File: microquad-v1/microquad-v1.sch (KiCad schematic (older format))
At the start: 20 parts

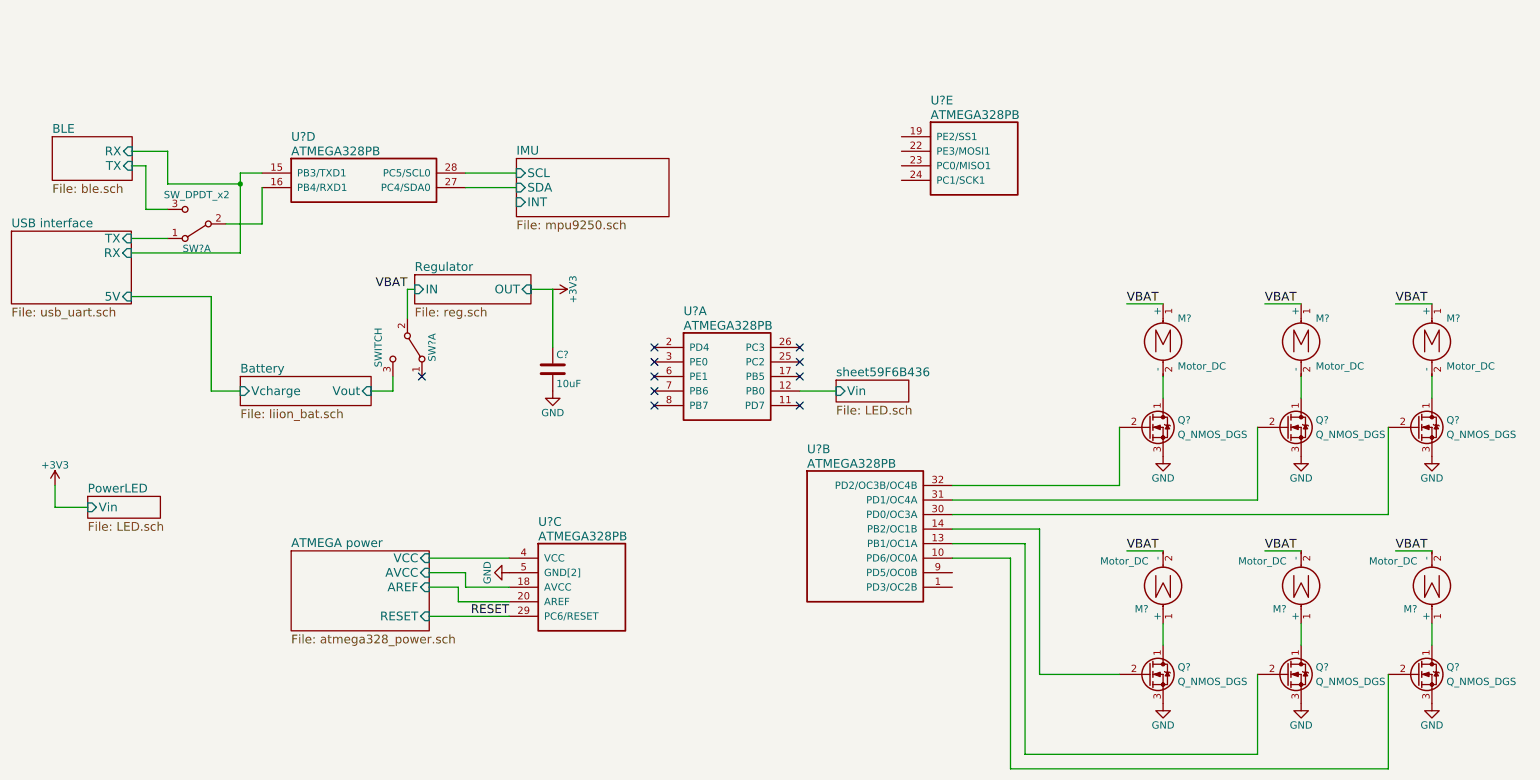
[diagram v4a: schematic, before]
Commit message: Moved LED to pin PB5
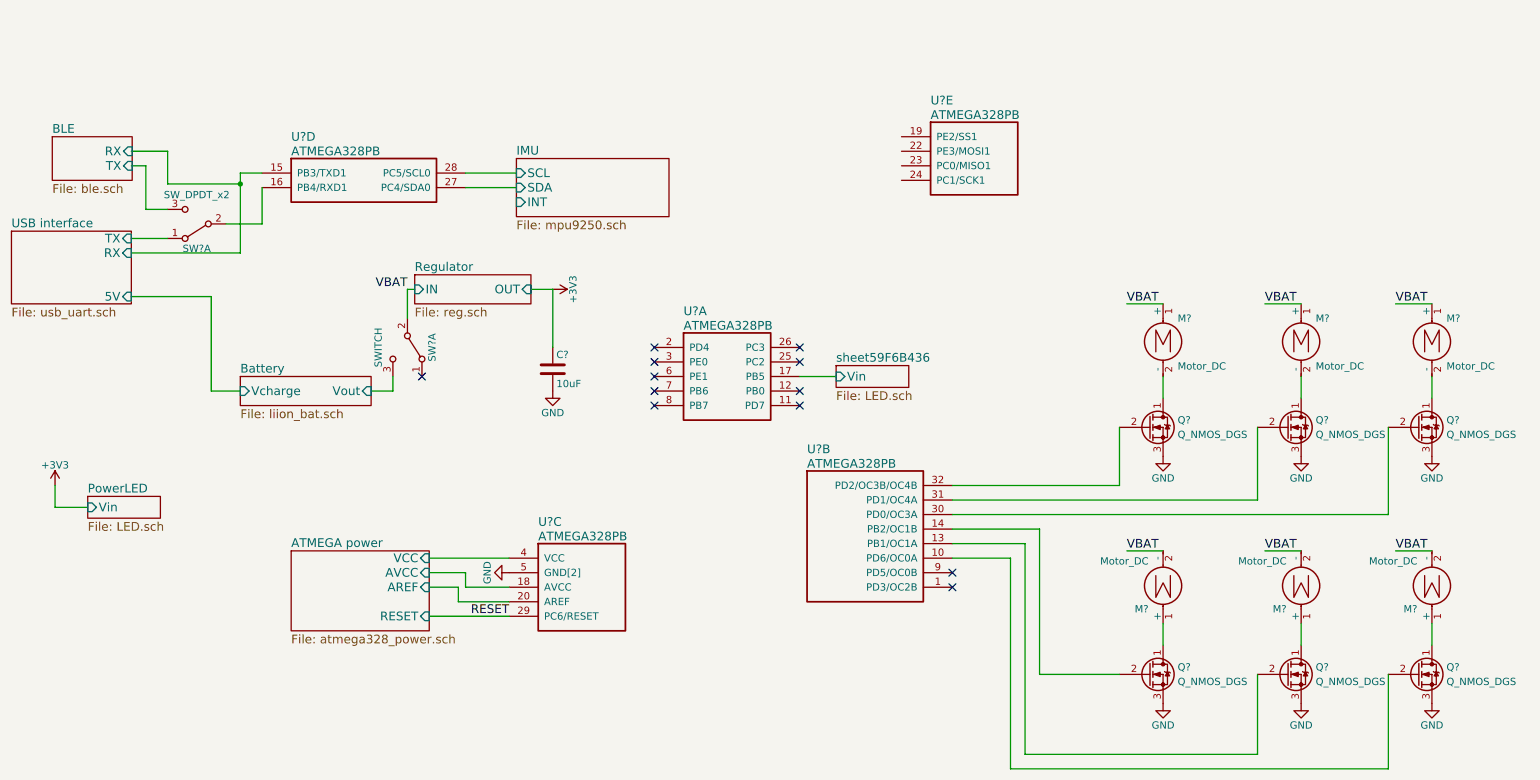
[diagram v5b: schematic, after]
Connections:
- wire segments 64 -> 63
- no-connect marks 10 -> 12
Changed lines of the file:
@@
 $Descr A4 11693 8268
 encoding utf-8
-Sheet 1 8
+Sheet 1 9
 Title ""
 Date ""
@@
 	10500 5000 10500 5150
 Wire Wire Line
-	6150 3400 6400 3400
-Wire Wire Line
 	8350 3650 8350 4050
 Wire Wire Line
@@
 	1800 1975 2300 1975
 Wire Wire Line
-	2300 1900 2300 1975
-Wire Wire Line
-	2300 1975 2300 2450
+	2300 1900 2300 2450
 Wire Wire Line
 	2300 1900 2450 1900
@@
 $EndSheet
 $Sheet
-S 6400 3325 500  150
+S 6400 3225 500  150
 U 59F6B438
 F0 "sheet59F6B436" 60
 F1 "LED.sch" 60
-F2 "Vin" I L 6400 3400 60
+F2 "Vin" I L 6400 3300 60
 $EndSheet
 $Comp
@@
 NoConn ~ 6150 3100
 NoConn ~ 6150 3200
-NoConn ~ 6150 3300
 NoConn ~ 6150 3500
 NoConn ~ 5150 3500
@@
 F4 "INT" I L 4200 2100 60
 $EndSheet
+NoConn ~ 7200 4650
+NoConn ~ 7200 4750
+NoConn ~ 6150 3400
+Wire Wire Line
+	6150 3300 6400 3300
 $EndSCHEMATC

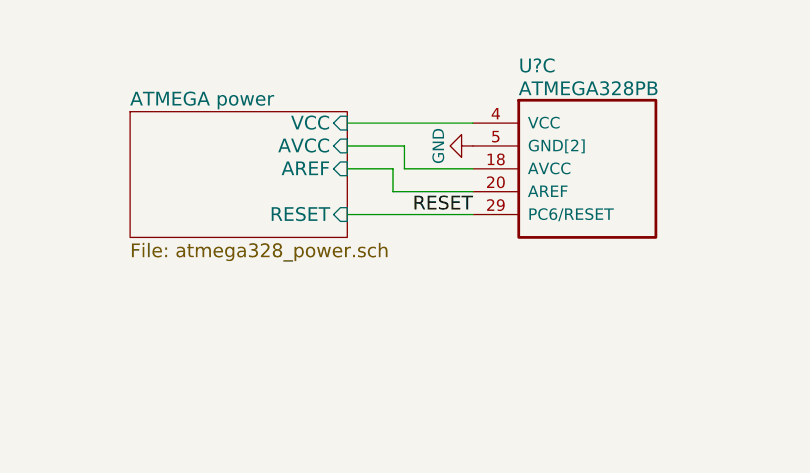
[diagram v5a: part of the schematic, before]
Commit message: Added reset button
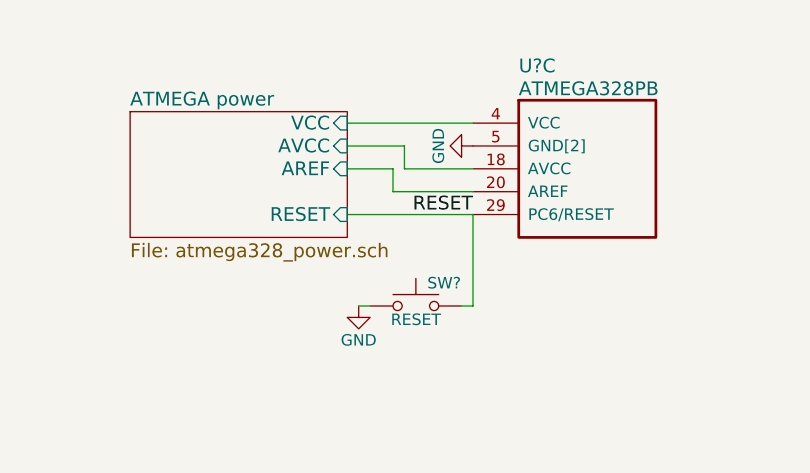
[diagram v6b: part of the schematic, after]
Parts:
- added SW?: RESET, symbol SW_Push
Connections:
- wire segments 63 -> 66
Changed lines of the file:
@@
 Wire Wire Line
 	6150 3300 6400 3300
+$Comp
+L SW_Push SW?
+U 1 1 59F7EEE0
+P 3900 5350
+F 0 "SW?" H 3950 5450 50  0000 L CNN
+F 1 "RESET" H 3900 5290 50  0000 C CNN
+F 2 "" H 3900 5550 50  0001 C CNN
+F 3 "" H 3900 5550 50  0001 C CNN
+	1    3900 5350
+	1    0    0    -1
+$EndComp
+$Comp
+L GND #PWR?
+U 1 1 59F7EFD3
+P 3650 5350
+F 0 "#PWR?" H 3650 5100 50  0001 C CNN
+F 1 "GND" H 3650 5200 50  0000 C CNN
+F 2 "" H 3650 5350 50  0001 C CNN
+F 3 "" H 3650 5350 50  0001 C CNN
+	1    3650 5350
+	1    0    0    -1
+$EndComp
+Wire Wire Line
+	3650 5350 3700 5350
+Wire Wire Line
+	4150 4950 4150 5350
+Wire Wire Line
+	4150 5350 4100 5350
 $EndSCHEMATC

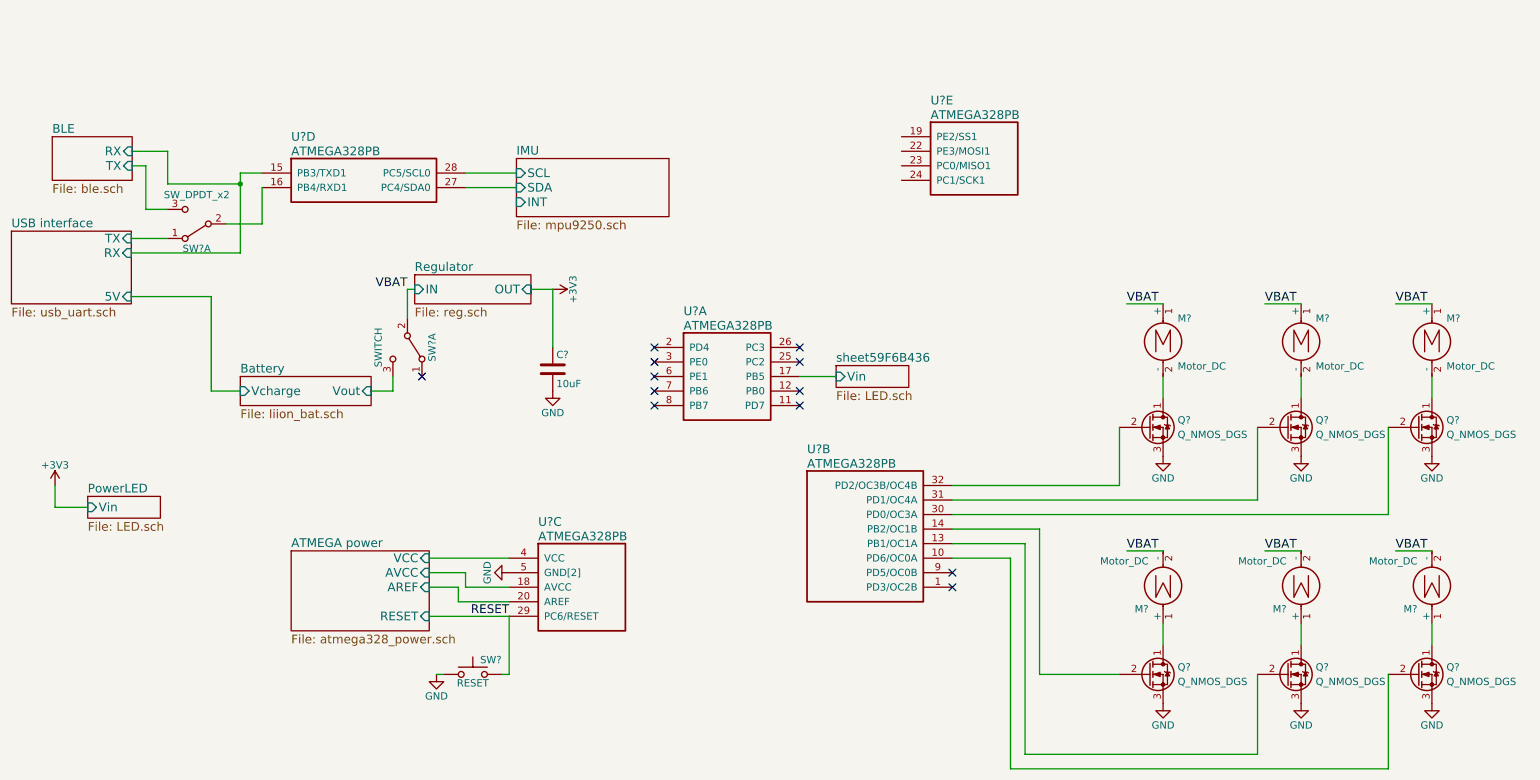
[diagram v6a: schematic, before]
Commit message: Added IMU interrupt
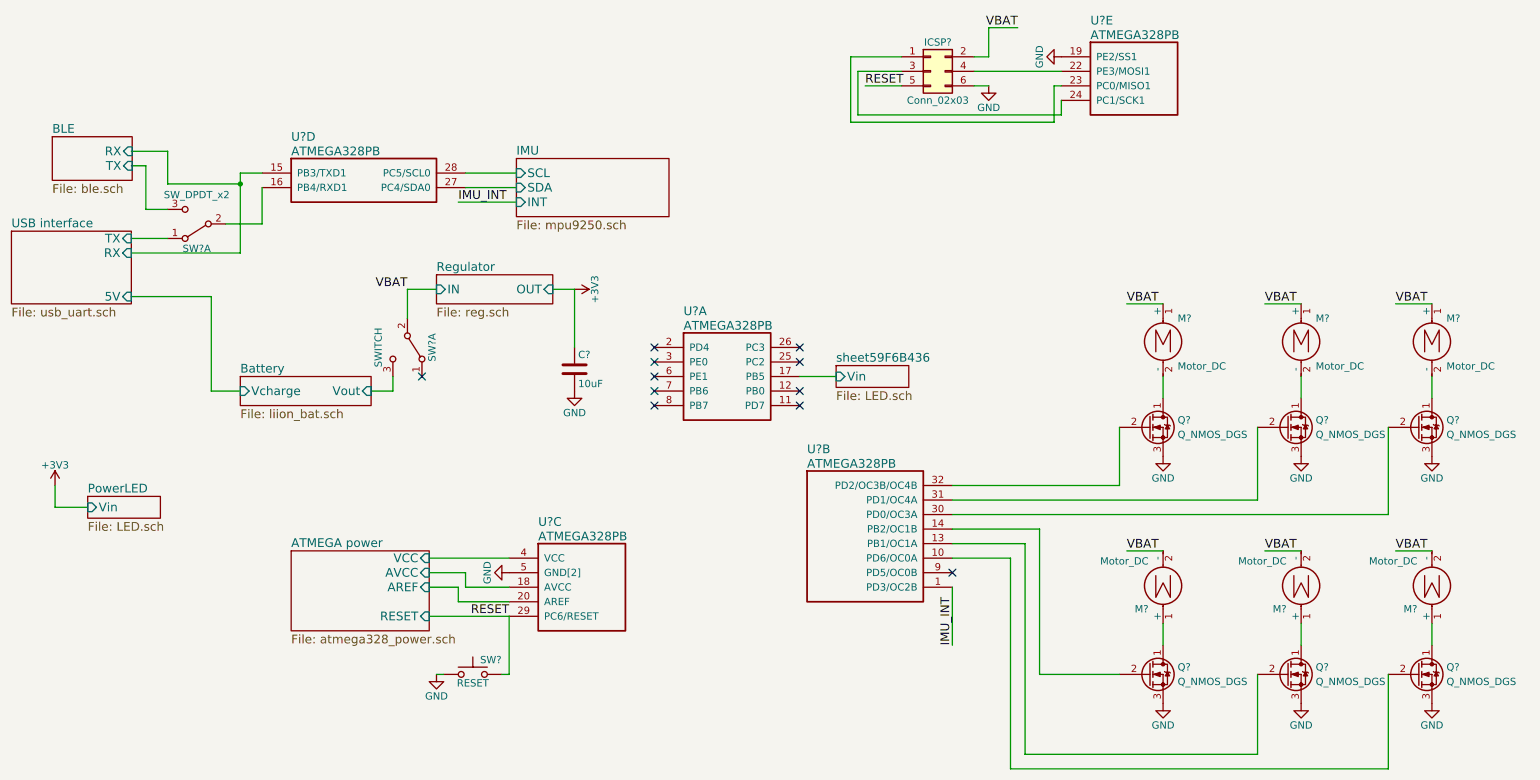
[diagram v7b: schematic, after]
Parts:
- added ICSP?: Conn_02x03, symbol Conn_02x03_Odd_Even
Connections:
- net GND: now also U?.19 (PE2/SS1), ICSP?.6 (Pin_6)
- net RESET: now also ICSP?.5 (Pin_5)
- net VBAT: now also ICSP?.2 (Pin_2)
- net IMU_INT: now reaches U?.1 (PD3/OC2B)
- net at U?.22 (PE3/MOSI1): now also ICSP?.4 (Pin_4)
- net at U?.23 (PC0/MISO1): now also ICSP?.1 (Pin_1)
- net at U?.24 (PC1/SCK1): now also ICSP?.3 (Pin_3)
- no-connect marks 12 -> 11
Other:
- moved on the sheet: C?, U?E
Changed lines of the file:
@@
 $EndDescr
 $Sheet
-S 3500 2600 800  200
+S 3650 2600 800  200
 U 59F2417D
 F0 "Regulator" 60
 F1 "reg.sch" 60
-F2 "OUT" I R 4300 2700 60
-F3 "IN" I L 3500 2700 60
+F2 "OUT" I R 4450 2700 60
+F3 "IN" I L 3650 2700 60
 $EndSheet
 $Sheet
@@
 L ATMEGA328PB U?
 U 5 1 59F275A9
-P 6850 1650
-F 0 "U?" H 7050 1900 60  0000 L CNN
-F 1 "ATMEGA328PB" H 7050 1800 60  0000 L CNN
-F 2 "" H 6850 1650 60  0001 C CNN
-F 3 "" H 6850 1650 60  0001 C CNN
-	5    6850 1650
+P 7950 1100
+F 0 "U?" H 8150 1350 60  0000 L CNN
+F 1 "ATMEGA328PB" H 8150 1250 60  0000 L CNN
+F 2 "" H 7950 1100 60  0001 C CNN
+F 3 "" H 7950 1100 60  0001 C CNN
+	5    7950 1100
 	1    0    0    -1
 $EndComp
@@
 L +3V3 #PWR02
 U 1 1 59F530BC
-P 4450 2700
-F 0 "#PWR02" H 4450 2550 50  0001 C CNN
-F 1 "+3V3" H 4450 2840 50  0000 C CNN
-F 2 "" H 4450 2700 50  0001 C CNN
-F 3 "" H 4450 2700 50  0001 C CNN
-	1    4450 2700
+P 4600 2700
+F 0 "#PWR02" H 4600 2550 50  0001 C CNN
+F 1 "+3V3" H 4600 2840 50  0000 C CNN
+F 2 "" H 4600 2700 50  0001 C CNN
+F 3 "" H 4600 2700 50  0001 C CNN
+	1    4600 2700
 	0    1    1    0
 $EndComp
@@
 L C C?
 U 1 1 59F54C39
-P 4450 3250
-F 0 "C?" H 4475 3350 50  0000 L CNN
-F 1 "10uF" H 4475 3150 50  0000 L CNN
-F 2 "Capacitors_SMD:C_0805" H 4488 3100 50  0001 C CNN
-F 3 "" H 4450 3250 50  0001 C CNN
-	1    4450 3250
+P 4600 3250
+F 0 "C?" H 4625 3350 50  0000 L CNN
+F 1 "10uF" H 4625 3150 50  0000 L CNN
+F 2 "Capacitors_SMD:C_0805" H 4638 3100 50  0001 C CNN
+F 3 "" H 4600 3250 50  0001 C CNN
+	1    4600 3250
 	1    0    0    -1
 $EndComp
@@
 L GND #PWR03
 U 1 1 59F54CA2
-P 4450 3400
-F 0 "#PWR03" H 4450 3150 50  0001 C CNN
-F 1 "GND" H 4450 3250 50  0000 C CNN
-F 2 "" H 4450 3400 50  0001 C CNN
-F 3 "" H 4450 3400 50  0001 C CNN
-	1    4450 3400
-	1    0    0    -1
-$EndComp
-Wire Wire Line
-	4450 2700 4450 3100
-Wire Wire Line
-	4450 2700 4300 2700
+P 4600 3400
+F 0 "#PWR03" H 4600 3150 50  0001 C CNN
+F 1 "GND" H 4600 3250 50  0000 C CNN
+F 2 "" H 4600 3400 50  0001 C CNN
+F 3 "" H 4600 3400 50  0001 C CNN
+	1    4600 3400
+	1    0    0    -1
+$EndComp
+Wire Wire Line
+	4600 2700 4600 3100
+Wire Wire Line
+	4600 2700 4450 2700
 $Sheet
 S 2300 3300 900  200
@@
 	3450 2900 3450 2700
 Wire Wire Line
-	3450 2700 3500 2700
+	3450 2700 3650 2700
 NoConn ~ 3550 3300
 $Sheet
@@
 $EndSheet
 NoConn ~ 7200 4650
-NoConn ~ 7200 4750
 NoConn ~ 6150 3400
 Wire Wire Line
@@
 Wire Wire Line
 	4150 5350 4100 5350
+$Comp
+L Conn_02x03_Odd_Even ICSP?
+U 1 1 59F84B16
+P 7050 1200
+F 0 "ICSP?" H 7100 1400 50  0000 C CNN
+F 1 "Conn_02x03" H 7100 1000 50  0000 C CNN
+F 2 "" H 7050 1200 50  0001 C CNN
+F 3 "" H 7050 1200 50  0001 C CNN
+	1    7050 1200
+	1    0    0    -1
+$EndComp
+Wire Wire Line
+	7350 1100 7450 1100
+Wire Wire Line
+	7450 1100 7450 900
+Wire Wire Line
+	7450 900  7650 900
+Text Label 7650 900  2    60   ~ 0
+VBAT
+Wire Wire Line
+	7350 1300 7450 1300
+$Comp
+L GND #PWR?
+U 1 1 59F8679D
+P 7450 1300
+F 0 "#PWR?" H 7450 1050 50  0001 C CNN
+F 1 "GND" H 7450 1150 50  0000 C CNN
+F 2 "" H 7450 1300 50  0001 C CNN
+F 3 "" H 7450 1300 50  0001 C CNN
+	1    7450 1300
+	1    0    0    -1
+$EndComp
+Wire Wire Line
+	7350 1200 7950 1200
+Wire Wire Line
+	6850 1200 6550 1200
+Wire Wire Line
+	6550 1200 6550 1500
+Wire Wire Line
+	6550 1500 7950 1500
+Wire Wire Line
+	7950 1500 7950 1400
+Wire Wire Line
+	7950 1300 7900 1300
+Wire Wire Line
+	7900 1300 7900 1550
+Wire Wire Line
+	7900 1550 6500 1550
+Wire Wire Line
+	6500 1550 6500 1100
+Wire Wire Line
+	6500 1100 6850 1100
+Wire Wire Line
+	6850 1300 6600 1300
+Text Label 6600 1300 0    60   ~ 0
+RESET
+$Comp
+L GND #PWR?
+U 1 1 59F8B068
+P 7950 1100
+F 0 "#PWR?" H 7950 850 50  0001 C CNN
+F 1 "GND" H 7950 950 50  0000 C CNN
+F 2 "" H 7950 1100 50  0001 C CNN
+F 3 "" H 7950 1100 50  0001 C CNN
+	1    7950 1100
+	0    1    1    0
+$EndComp
+Wire Wire Line
+	4200 2100 3800 2100
+Text Label 3800 2100 0    60   ~ 0
+IMU_INT
+Text Label 7200 5150 1    60   ~ 0
+IMU_INT
+Wire Wire Line
+	7200 4750 7200 5150
 $EndSCHEMATC

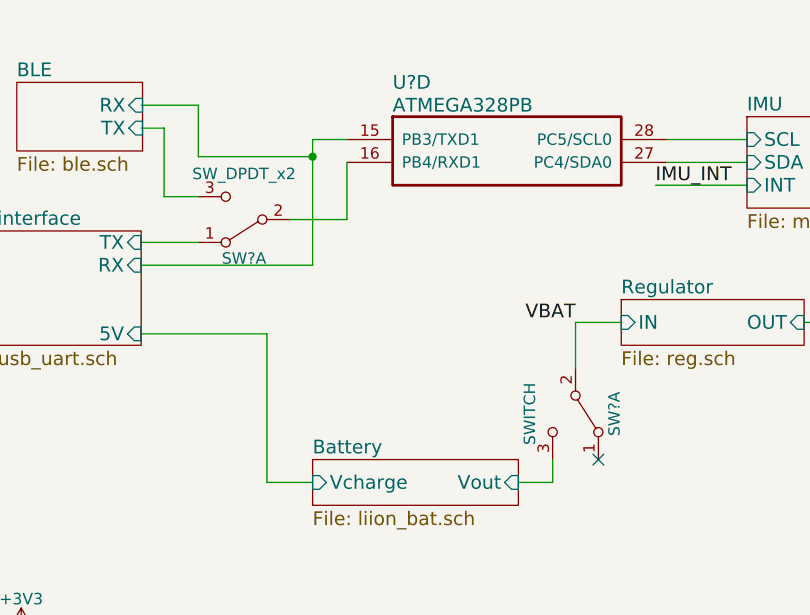
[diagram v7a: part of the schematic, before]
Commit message: Changed switches to SPDT to prevent erroneous assignment
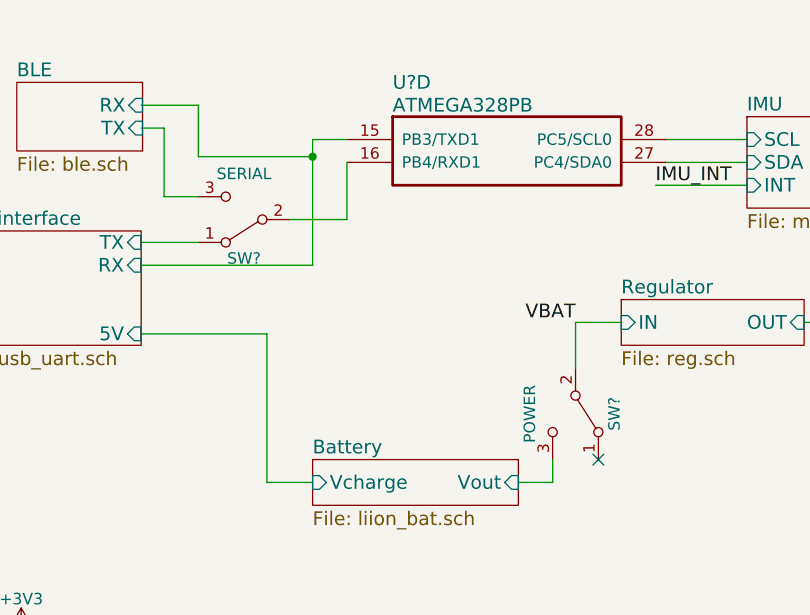
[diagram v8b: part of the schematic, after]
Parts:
- removed SW?: SWITCH, symbol SW_DPDT_x2
- removed SW?: SW_DPDT_x2, symbol SW_DPDT_x2
- added SW?: POWER, symbol SW_SPDT
- added SW?: SERIAL, symbol SW_SPDT
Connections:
- net Battery/Vout: now also SW?.3 (C)
- net USB interface/TX: now also SW?.1 (A)
- net VBAT: now also SW?.2 (B)
- net at U?.16 (PB4/RXD1): now also SW?.2 (B)
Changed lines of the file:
@@
 Text Label 3450 2700 2    60   ~ 0
 VBAT
-$Comp
-L SW_DPDT_x2 SW?
-U 1 1 59F60CDA
-P 3450 3100
-F 0 "SW?" H 3450 3270 50  0000 C CNN
-F 1 "SWITCH" H 3450 2900 50  0000 C CNN
-F 2 "" H 3450 3100 50  0001 C CNN
-F 3 "" H 3450 3100 50  0001 C CNN
-	1    3450 3100
-	0    1    1    0
-$EndComp
 Wire Wire Line
 	3350 3400 3350 3300
@@
 Wire Wire Line
 	7600 4550 7200 4550
-$Comp
-L SW_DPDT_x2 SW?
-U 1 1 59F6779C
-P 2000 2250
-F 0 "SW?" H 2000 2420 50  0000 C CNN
-F 1 "SW_DPDT_x2" H 2000 2050 50  0000 C CNN
-F 2 "" H 2000 2250 50  0001 C CNN
-F 3 "" H 2000 2250 50  0001 C CNN
-	1    2000 2250
-	-1   0    0    1
-$EndComp
 Wire Wire Line
 	1550 1850 1650 1850
@@
 Wire Wire Line
 	7200 4750 7200 5150
+$Comp
+L SW_SPDT SW?
+U 1 1 59F9E6E3
+P 3450 3100
+F 0 "SW?" H 3450 3270 50  0000 C CNN
+F 1 "POWER" H 3450 2900 50  0000 C CNN
+F 2 "" H 3450 3100 50  0001 C CNN
+F 3 "" H 3450 3100 50  0001 C CNN
+	1    3450 3100
+	0    1    1    0
+$EndComp
+$Comp
+L SW_SPDT SW?
+U 1 1 59F9E9A3
+P 2000 2250
+F 0 "SW?" H 2000 2420 50  0000 C CNN
+F 1 "SERIAL" H 2000 2050 50  0000 C CNN
+F 2 "" H 2000 2250 50  0001 C CNN
+F 3 "" H 2000 2250 50  0001 C CNN
+	1    2000 2250
+	-1   0    0    1
+$EndComp
 $EndSCHEMATC
